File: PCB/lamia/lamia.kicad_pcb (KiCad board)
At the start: 2 copper layers, 111.6 x 76 mm, 30 parts

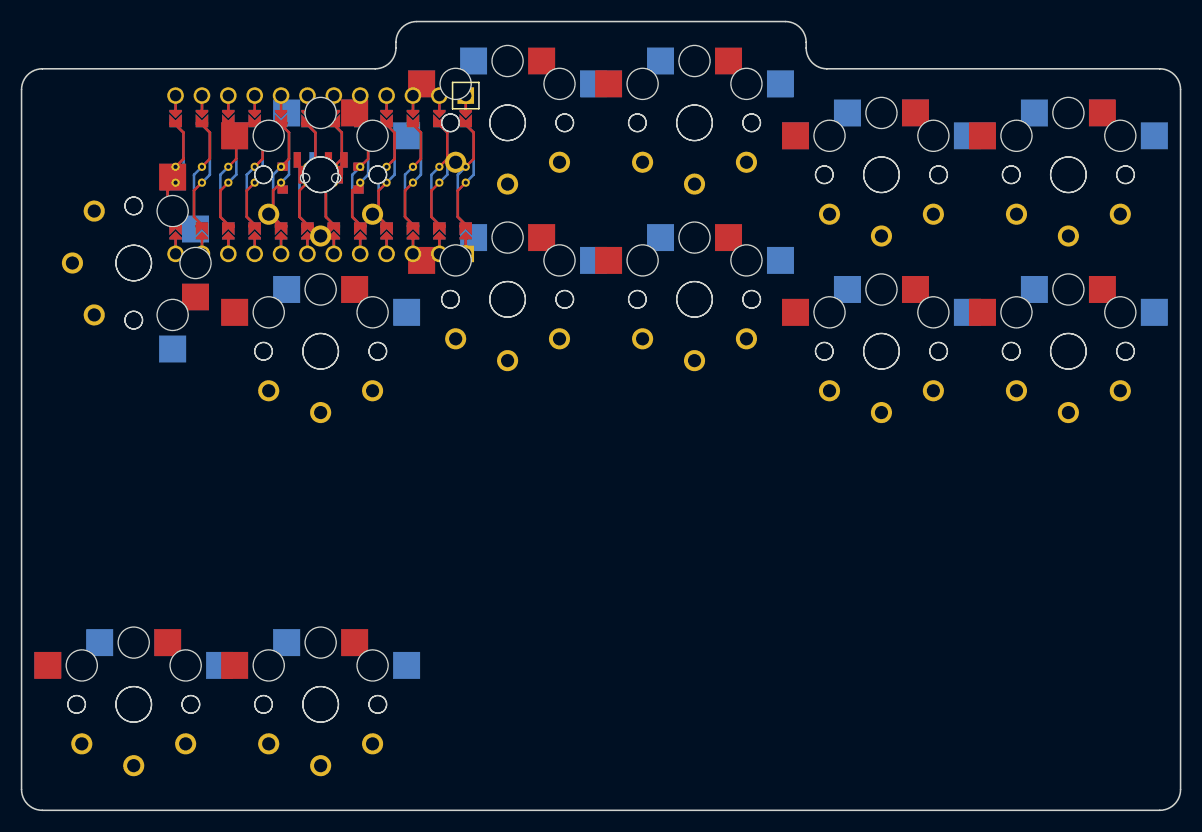
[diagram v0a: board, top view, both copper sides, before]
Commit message: all pcb nets set
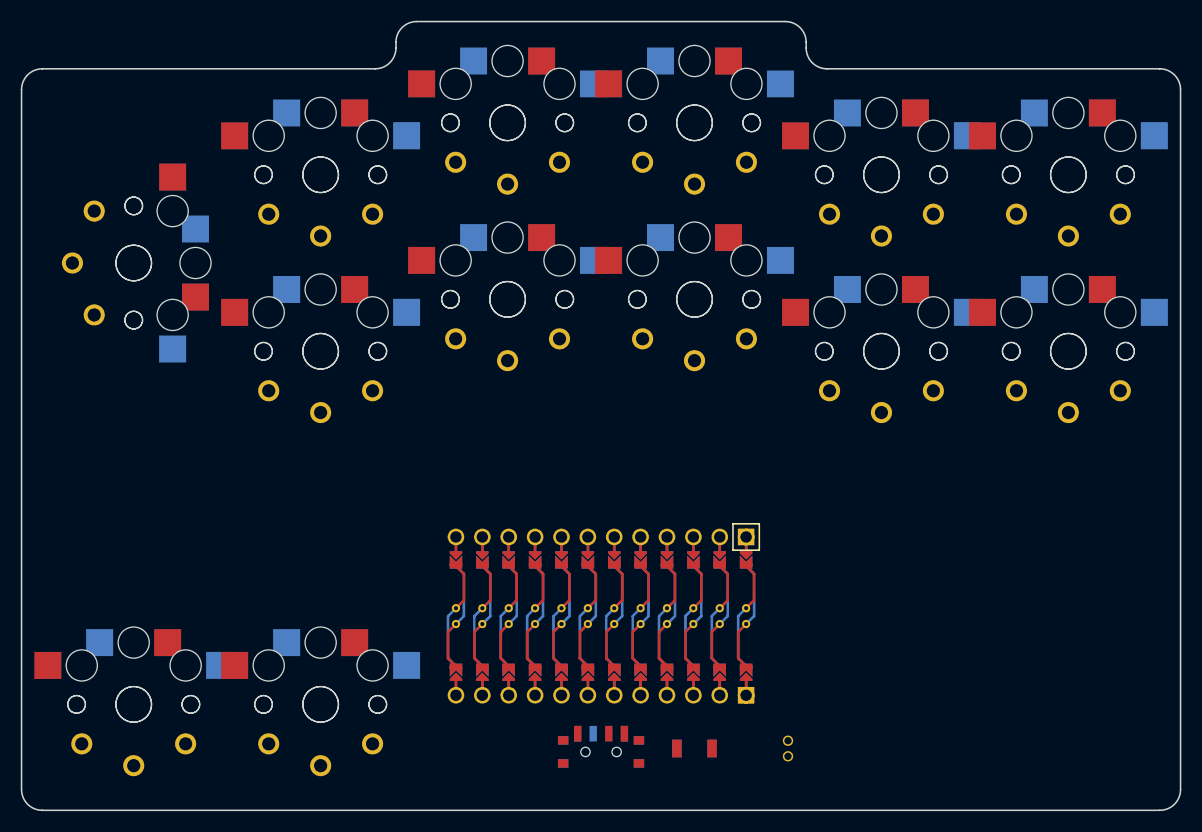
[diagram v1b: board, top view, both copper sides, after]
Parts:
- moved ? 71.3 mm to (63.0, 46.8)
- moved ? 65.9 mm to (54.0, 46.8)
- moved ? 61.5 mm to (45.0, 46.8)
- moved MCU1 50.4 mm to (45.0, 34.0)
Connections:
- S10 pad 1: P9 -> P6
- S11 pad 1: P9 -> P18
- S12 pad 1: P9 -> P18
- S13 pad 1: P9 -> P5
- S14 pad 1: P9 -> P5
- S15 pad 1: P9 -> P19
- S16 pad 1: P9 -> P19
- S17 pad 1: P9 -> P4
- S18 pad 1: P9 -> P4
- S19 pad 1: P9 -> P21
- S20 pad 1: P9 -> P21
- S21 pad 1: P9 -> P20
- S22 pad 1: P9 -> P20
- S23 pad 1: P9 -> P10
- S24 pad 1: P9 -> P10
- S25 pad 1: P9 -> P16
- S26 pad 1: P9 -> P16
- S3 pad 1: P9 -> P8
- S4 pad 1: P9 -> P8
- S5 pad 1: P9 -> P7
- S6 pad 1: P9 -> P7
- S7 pad 1: P9 -> P15
- S8 pad 1: P9 -> P15
- S9 pad 1: P9 -> P6
